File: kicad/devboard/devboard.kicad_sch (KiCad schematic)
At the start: 24 parts, among them J1 USB_C_Receptacle, J2 Conn_01x04_Socket, SW1 SW_Push, SW2 SW_Push, U2 CH340G, U3 STM32G030K8Tx, Y1 12 MHz, Y2 8MHz resonator

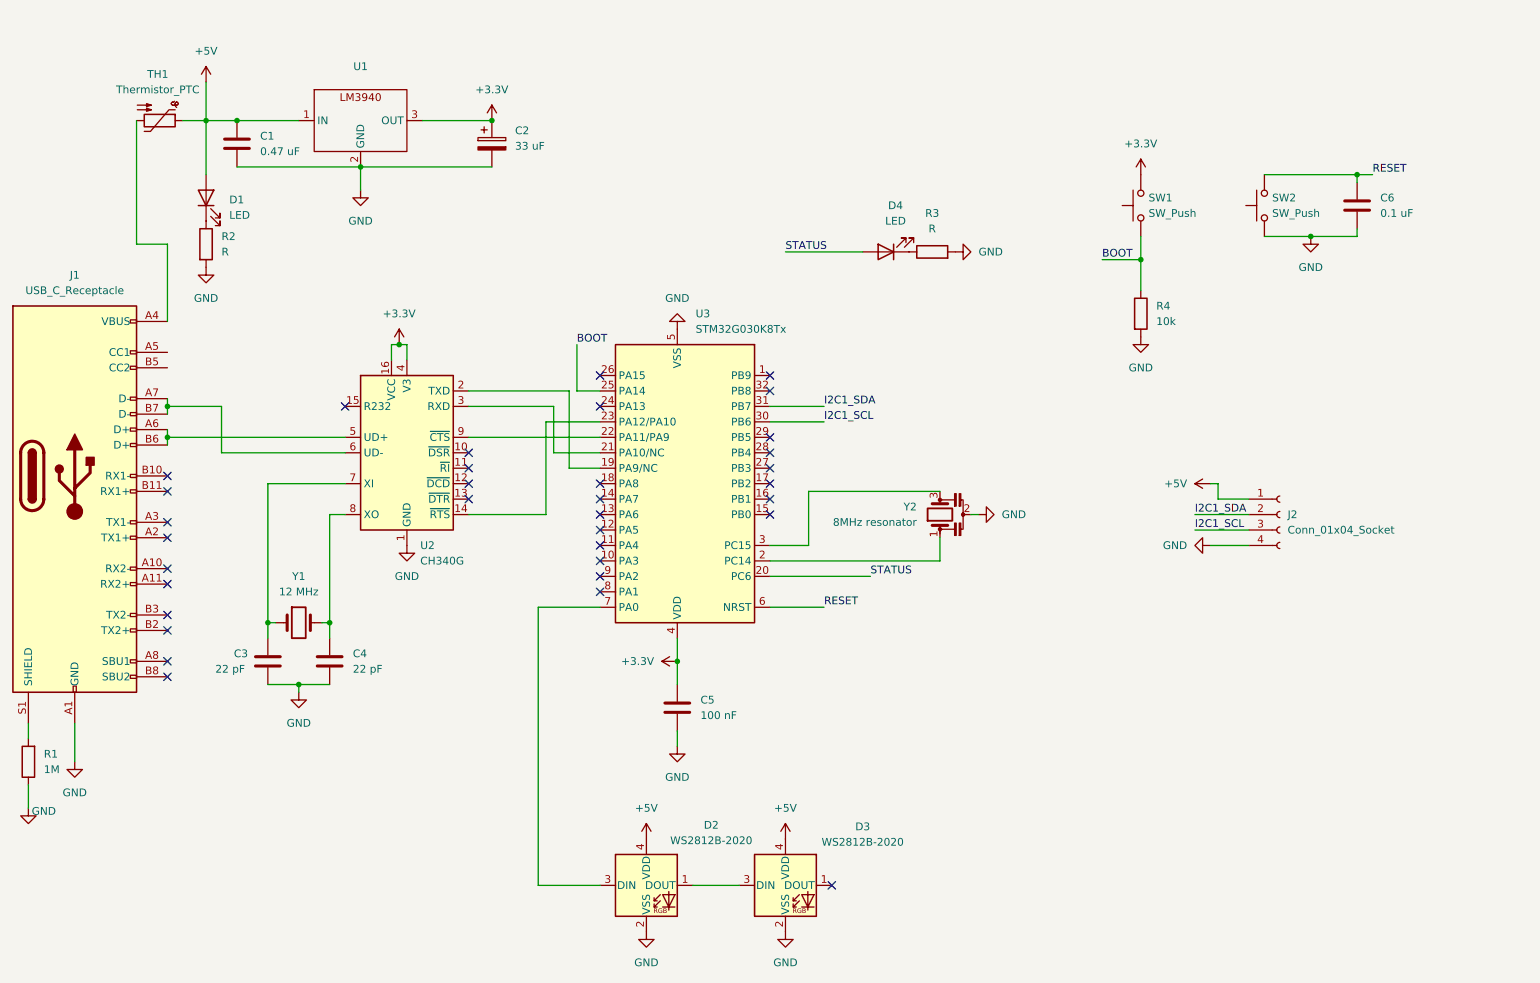
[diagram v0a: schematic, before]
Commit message: added many many footprints
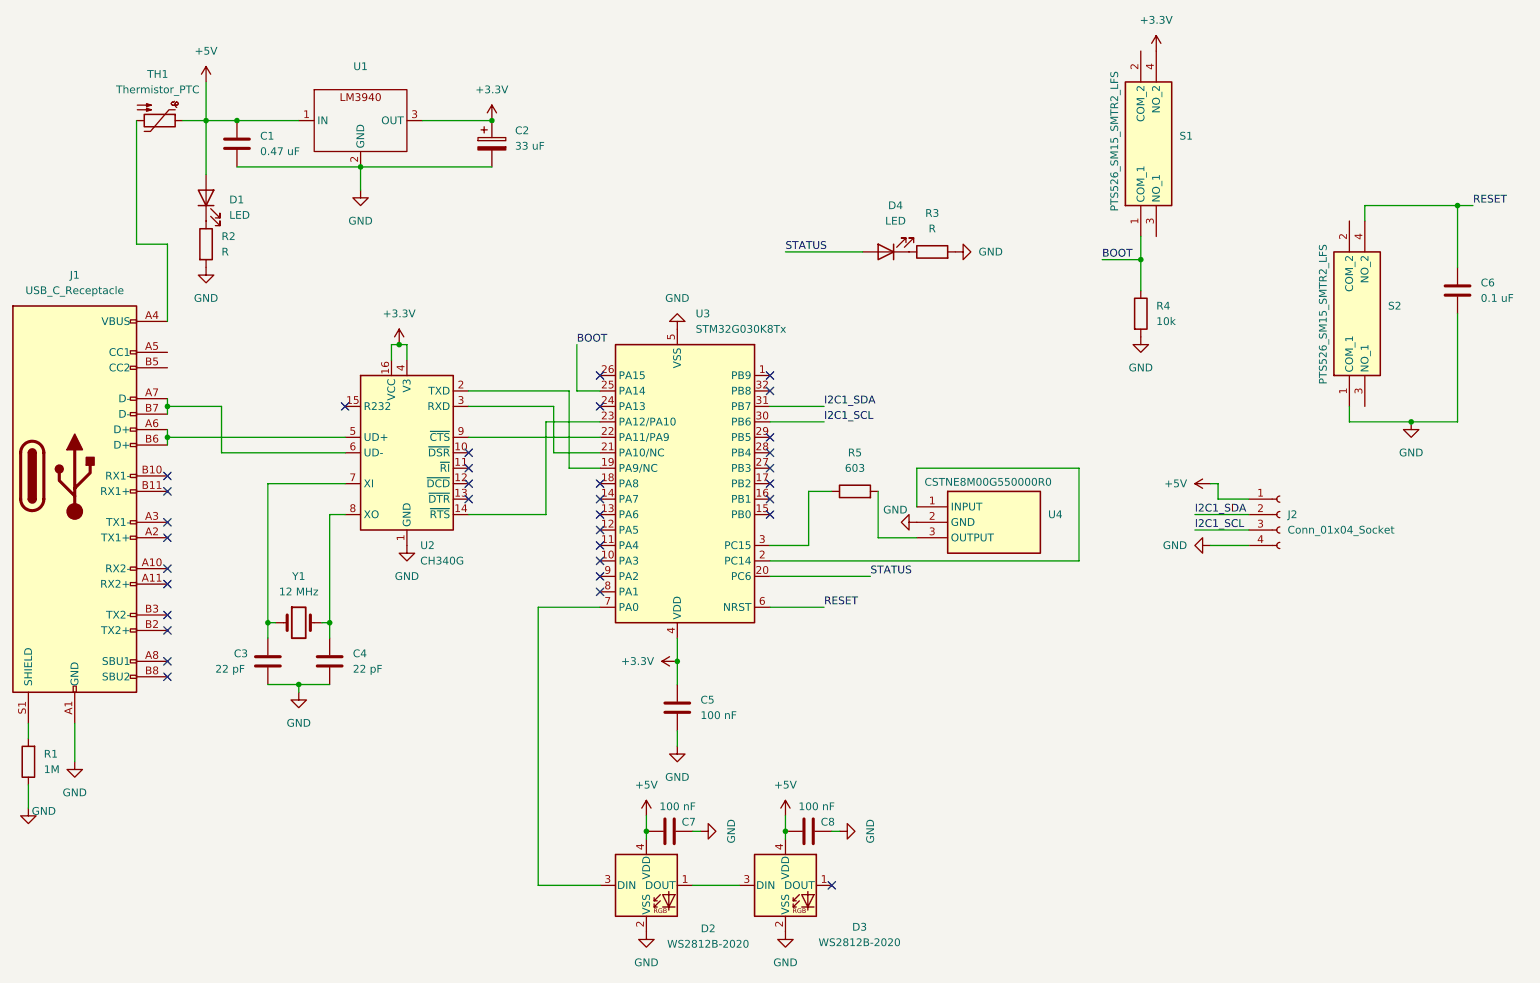
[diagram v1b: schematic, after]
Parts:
- removed SW1, SW2: SW_Push, symbol Switch:SW_Push
- removed Y2: 8MHz resonator, symbol Device:Resonator
- added C7, C8: 100 nF, Capacitor_SMD:C_0201_0603Metric, symbol Device:C
- added R5: 603, Resistor_SMD:R_0201_0603Metric, symbol Device:R
- added S1, S2: PTS526_SM15_SMTR2_LFS, mesonlib:PTS526SM15SMTR2LFS, symbol mesonlib:PTS526_SM15_SMTR2_LFS
- added U4: CSTNE8M00G550000R0, mesonlib:CSTNE16M0V530000R0, symbol mesonlib:CSTNE8M00G550000R0
- C1, C2, C3, C4, C5, C6: footprint (none) -> Capacitor_SMD:C_0201_0603Metric
- J1: footprint (none) -> Connector_USB:USB_C_Receptacle_Molex_105450-0101
- J2: footprint (none) -> Connector_PinHeader_1.00mm:PinHeader_1x04_P1.00mm_Vertical_SMD_Pin1Right
- R1, R2, R3, R4, Y1: footprint (none) -> Resistor_SMD:R_0201_0603Metric
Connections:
- net +3.3V: now also S1.4 (NO_2)
- net +5V: now also C7.1, C8.1
- net BOOT: now also S1.1 (COM_1)
- net GND: now also C7.2, C8.2, S2.1 (COM_1), U4.2 (GND)
- net RESET: now also S2.4 (NO_2)
- net at U3.2 (PC14): now also U4.1 (INPUT)
- net at U3.3 (PC15): now also R5.1
- new net: R5.2, U4.3 (OUTPUT)
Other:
- moved on the sheet: C6

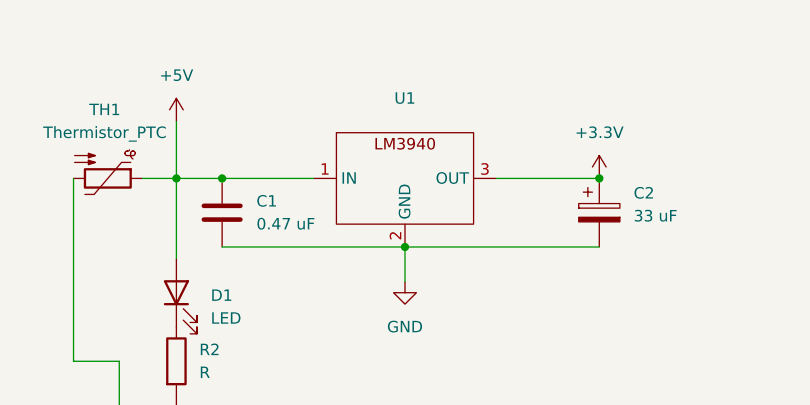
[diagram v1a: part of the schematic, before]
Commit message: all but thermistor footprint added
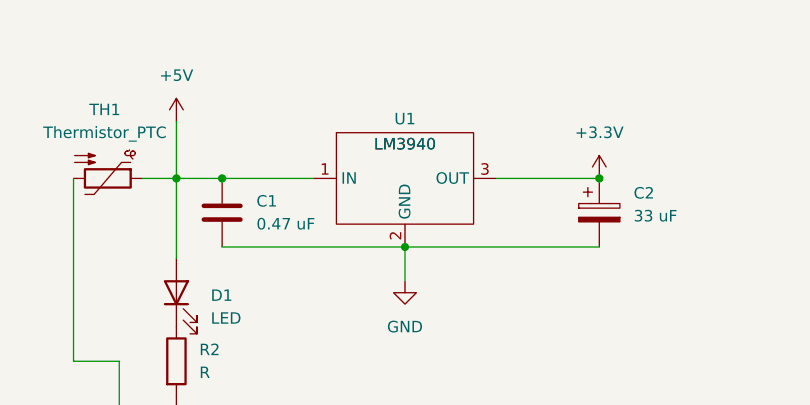
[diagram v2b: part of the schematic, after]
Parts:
- C1, C2, C3, C4, C5, C6, C7, C8: footprint Capacitor_SMD:C_0201_0603Metric -> Capacitor_SMD:C_0603_1608Metric
- D1, D4: footprint (none) -> Diode_SMD:D_0603_1608Metric
- R1, R2, R3, R4, R5, Y1: footprint Resistor_SMD:R_0201_0603Metric -> Resistor_SMD:R_0603_1608Metric
- U1: value ~ -> LM3940; footprint (none) -> mesonlib:LM3940
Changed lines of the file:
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@@
 			)
 		)
-		(property "Footprint" "Capacitor_SMD:C_0201_0603Metric"
+		(property "Footprint" "Capacitor_SMD:C_0603_1608Metric"
 			(at 72.0852 124.46 0)
 			(effects
@@
 			)
 		)
-		(property "Footprint" "Resistor_SMD:R_0201_0603Metric"
+		(property "Footprint" "Resistor_SMD:R_0603_1608Metric"
 			(at 157.48 94.488 90)
 			(effects
@@
 			)
 		)
-		(property "Footprint" "Resistor_SMD:R_0201_0603Metric"
+		(property "Footprint" "Resistor_SMD:R_0603_1608Metric"
 			(at 202.692 63.5 90)
 			(effects
@@
 			)
 		)
-		(property "Footprint" "Capacitor_SMD:C_0201_0603Metric"
+		(property "Footprint" "Capacitor_SMD:C_0603_1608Metric"
 			(at 98.7552 39.37 0)
 			(effects
@@
 			)
 		)
-		(property "Footprint" "Capacitor_SMD:C_0201_0603Metric"
+		(property "Footprint" "Capacitor_SMD:C_0603_1608Metric"
 			(at 130.81 147.6248 0)
 			(effects
@@
 			)
 		)
-		(property "Footprint" "Resistor_SMD:R_0201_0603Metric"
+		(property "Footprint" "Resistor_SMD:R_0603_1608Metric"
 			(at 170.18 55.118 90)
 			(effects
@@
 			)
 		)
-		(property "Footprint" "Resistor_SMD:R_0201_0603Metric"
+		(property "Footprint" "Resistor_SMD:R_0603_1608Metric"
 			(at 23.368 137.16 90)
 			(effects
@@
 			)
 		)
-		(property "Footprint" ""
+		(property "Footprint" "Diode_SMD:D_0603_1608Metric"
 			(at 50.8 44.45 0)
 			(effects
@@
 			)
 		)
-		(property "Footprint" ""
+		(property "Footprint" "Diode_SMD:D_0603_1608Metric"
 			(at 162.56 53.34 0)
 			(effects
@@
 			)
 		)
-		(property "Footprint" "Capacitor_SMD:C_0201_0603Metric"
+		(property "Footprint" "Capacitor_SMD:C_0603_1608Metric"
 			(at 129.2352 132.08 0)
 			(effects
@@
 			)
 		)
-		(property "Footprint" "Resistor_SMD:R_0201_0603Metric"
+		(property "Footprint" "Resistor_SMD:R_0603_1608Metric"
 			(at 66.04 114.3 0)
 			(effects
@@
 			)
 		)
-		(property "Footprint" "Resistor_SMD:R_0201_0603Metric"
+		(property "Footprint" "Resistor_SMD:R_0603_1608Metric"
 			(at 49.022 52.07 90)
 			(effects
@@
 			)
 		)
-		(property "Footprint" "Capacitor_SMD:C_0201_0603Metric"
+		(property "Footprint" "Capacitor_SMD:C_0603_1608Metric"
 			(at 61.9252 124.46 0)
 			(effects
@@
 			)
 		)
-		(property "Footprint" "Capacitor_SMD:C_0201_0603Metric"
+		(property "Footprint" "Capacitor_SMD:C_0603_1608Metric"
 			(at 257.5052 63.5 0)
 			(effects
@@
 			)
 		)
-		(property "Footprint" "Capacitor_SMD:C_0201_0603Metric"
+		(property "Footprint" "Capacitor_SMD:C_0603_1608Metric"
 			(at 56.8452 39.37 0)
 			(effects
@@
 			)
 		)
-		(property "Footprint" "Capacitor_SMD:C_0201_0603Metric"
+		(property "Footprint" "Capacitor_SMD:C_0603_1608Metric"
 			(at 153.67 147.6248 0)
 			(effects
@@
 		(on_board yes)
 		(dnp no)
-		(fields_autoplaced yes)
 		(property "Reference" "U1"
-			(at 76.2 22.86 0)
+			(at 76.2 25.146 0)
 			(effects
 				(font
@@
 			)
 		)
-		(property "Value" "~"
-			(at 76.2 25.4 0)
+		(property "Value" "LM3940"
+			(at 76.2 27.94 0)
 			(effects
 				(font
@@
 			)
 		)
-		(property "Footprint" ""
+		(property "Footprint" "mesonlib:LM3940"
 			(at 76.2 31.75 0)
 			(effects

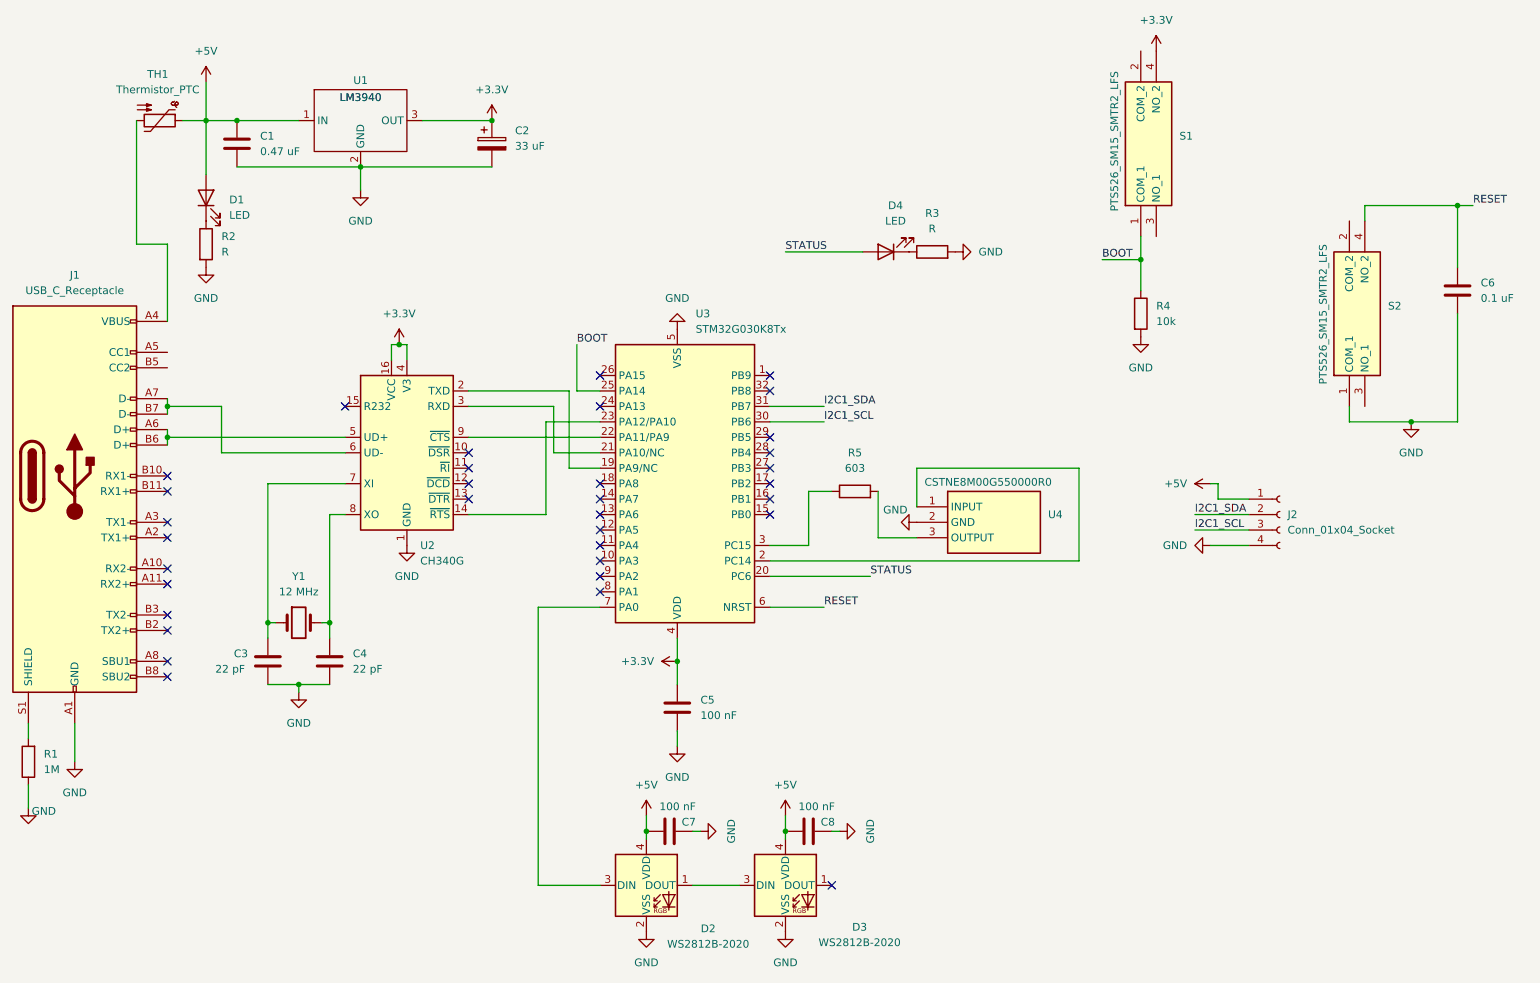
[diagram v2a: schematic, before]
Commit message: Updated footprint assignments and schematic
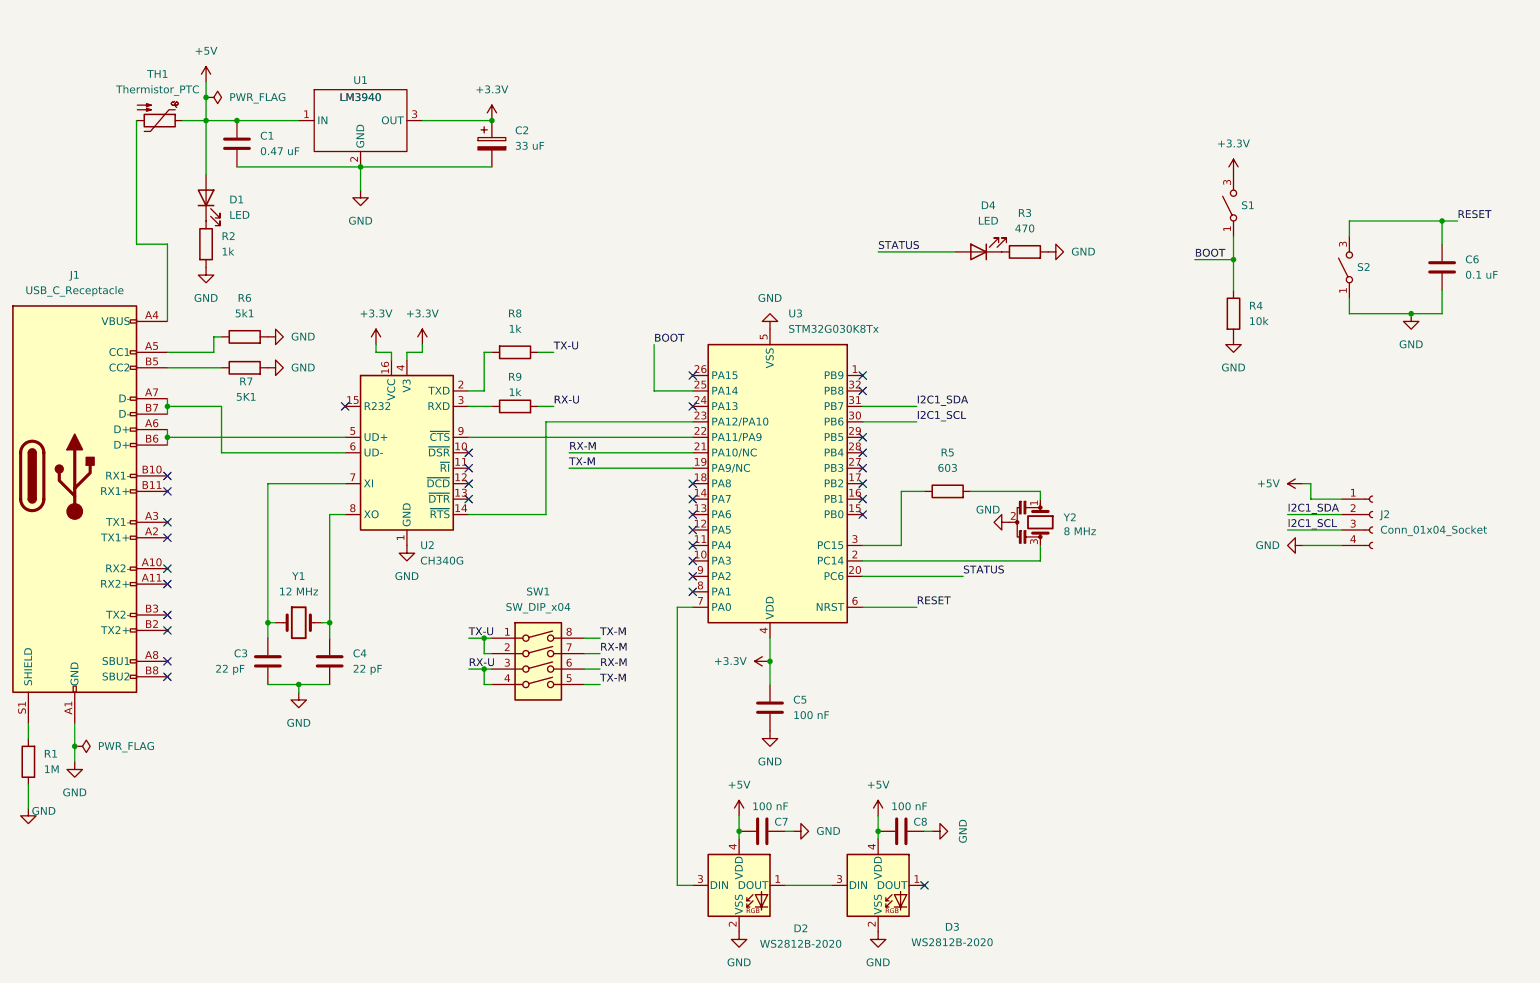
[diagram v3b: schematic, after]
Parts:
- removed S1, S2: PTS526_SM15_SMTR2_LFS, mesonlib:PTS526SM15SMTR2LFS, symbol mesonlib:PTS526_SM15_SMTR2_LFS
- added R6: 5k1, Resistor_SMD:R_0603_1608Metric, symbol Device:R
- added R7: 5K1, Resistor_SMD:R_0603_1608Metric, symbol Device:R
- added R8, R9: 1k, Resistor_SMD:R_0603_1608Metric, symbol Device:R
- added S1, S2: ~, mesonlib:PTS526SM15SMTR2LFS, symbol mesonlib:pushbutton_5.2x5.2mm_smd
- added SW1: SW_DIP_x04, Button_Switch_SMD:SW_DIP_SPSTx04_Slide_9.78x12.34mm_W8.61mm_P2.54mm, symbol Switch:SW_DIP_x04
- D1, D4: footprint Diode_SMD:D_0603_1608Metric -> LED_SMD:LED_0603_1608Metric
- J1: footprint Connector_USB:USB_C_Receptacle_Molex_105450-0101 -> Connector_USB:USB_C_Receptacle_Palconn_UTC16-G
- J2: footprint Connector_PinHeader_1.00mm:PinHeader_1x04_P1.00mm_Vertical_SMD_Pin1Right -> Connector_PinHeader_1.00mm:PinHeader_1x04_P1.00mm_Vertical
- R2: value R -> 1k
- R3: value R -> 470
- Y2: renamed from U4; value CSTNE8M00G550000R0 -> 8 MHz
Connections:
- net +3.3V: now also S1.3, S1.4
- net BOOT: now also S1.1, S1.2
- net GND: now also R6.2, R7.2, S2.1, S2.2
- net RESET: now also S2.3, S2.4
- net at J1.A5 (CC1): now also R6.1
- net at J1.B5 (CC2): now also R7.1
- net at R5.2: now also Y2.1; no longer Y2.3 (OUTPUT)
- net at U3.2 (PC14): now also Y2.3; no longer Y2.1 (INPUT)
- net at U2.2 (TXD): now also R8.2; no longer U3.19 (PA9/NC)
- net at U2.3 (RXD): now also R9.1; no longer U3.21 (PA10/NC)
- new net RX-M: SW1.6, SW1.7, U3.21 (PA10/NC)
- new net RX-U: R9.2, SW1.3, SW1.4
- new net TX-M: SW1.5, SW1.8, U3.19 (PA9/NC)
- new net TX-U: R8.1, SW1.1, SW1.2
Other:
- moved on the sheet: C5, C6, C7, C8, D2, D3, D4, J2, R3, R4, R5, U3
